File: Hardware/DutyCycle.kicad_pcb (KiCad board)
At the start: 2 copper layers, 40 x 20 mm, 42 parts, among them J1 LiPo, J2 USB, J4 MOT, Q1 AO3400A, Q2 AO3400A, Q3 AO3401A, SW1 SW_Push, U1 AT32F421KxU7, U3 ME6211C28M5, U5 TP4055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

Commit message: fix(Hardware): change the crystal starting capacitance 10pF -> 12pF
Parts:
- C10, C11: value 10pF -> 12pF

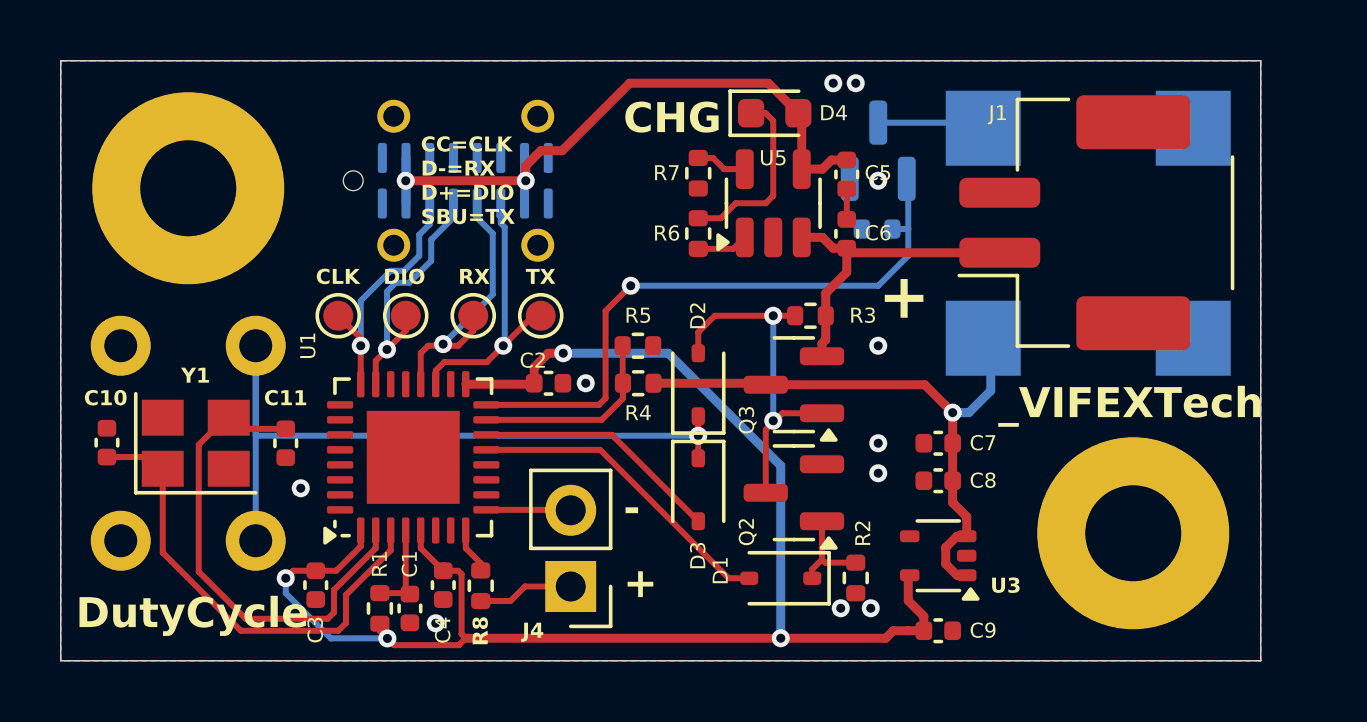
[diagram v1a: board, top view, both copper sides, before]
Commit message: feat(Hardware): add CH340E
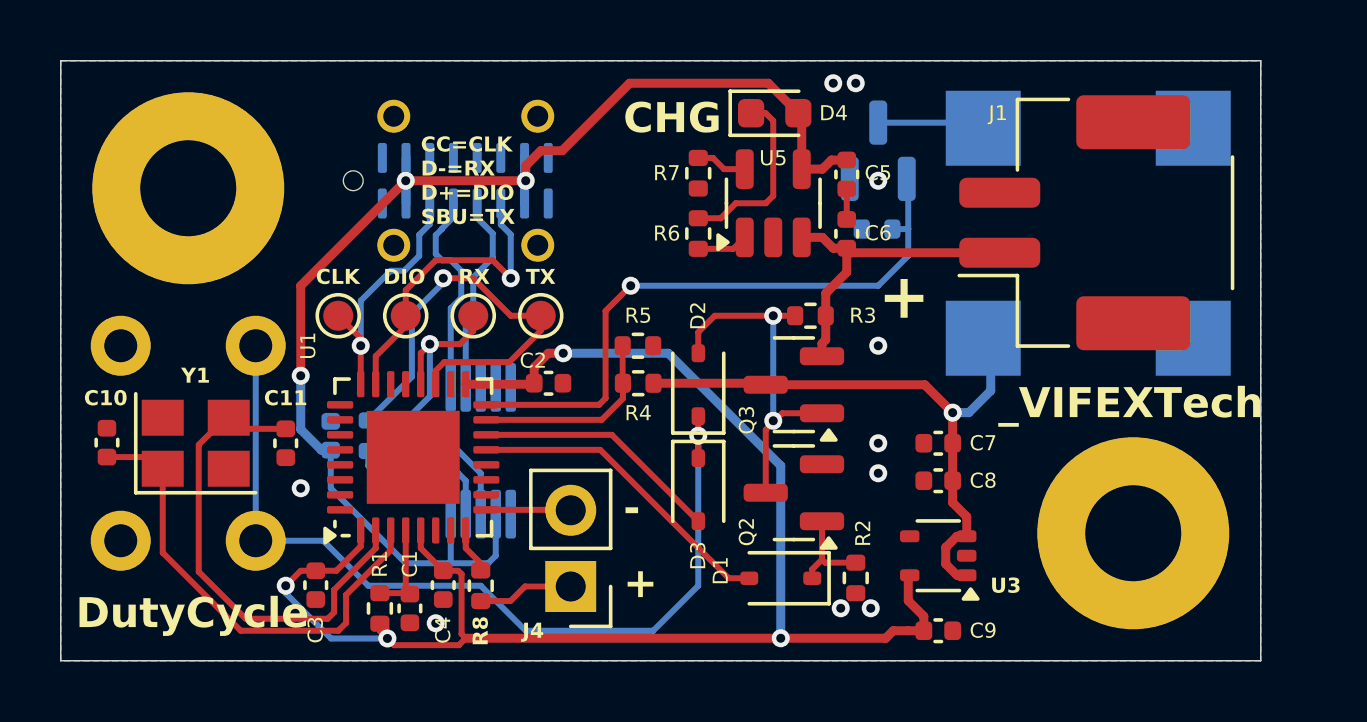
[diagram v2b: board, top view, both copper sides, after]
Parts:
- added C12: 100nF, Capacitor_SMD:C_0402_1005Metric, B.Cu at (84.0, 87.5)
- added R10: 10kR, Resistor_SMD:R_0402_1005Metric, B.Cu at (86.5, 87.5)
- added R11: 10kR, Resistor_SMD:R_0402_1005Metric, B.Cu at (85.2, 87.5)
- added U2: CH340E, Package_SO:MSOP-10_3x3mm_P0.5mm, B.Cu at (89.0, 88.0)
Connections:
- J2 pad A6: /SWDIO -> /UD+
- J2 pad A7: /DEBUG_RX -> /UD-
- J2 pad A8: /DEBUG_TX -> /SWDIO
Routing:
- net VBUS: track 21.8 -> 43.6 mm, vias 2 -> 3
- net /UD+: track 0.00 -> 7.04 mm
- net /UD-: track 0.00 -> 6.72 mm
- net Net-(U2-RXD): track 0.00 -> 5.06 mm
- net /DEBUG_TX: track 9.52 -> 14.5 mm
- net Net-(U2-TXD): track 0.00 -> 4.17 mm
- net Net-(D2-K): track 25.7 -> 29.5 mm
- net /DEBUG_RX: track 9.94 -> 6.97 mm
- net /SWDIO: track 8.80 -> 9.99 mm
- net /SWCLK: track 9.61 -> 8.90 mm
- net /HEXT_OUT: track 16.2 -> 15.6 mm
- net /HEXT_IN: track 15.8 -> 15.3 mm
- net GND: track 1.07 -> 1.02 mm, vias 11 -> 10

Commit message: fix(pcb): fix silk screen errors
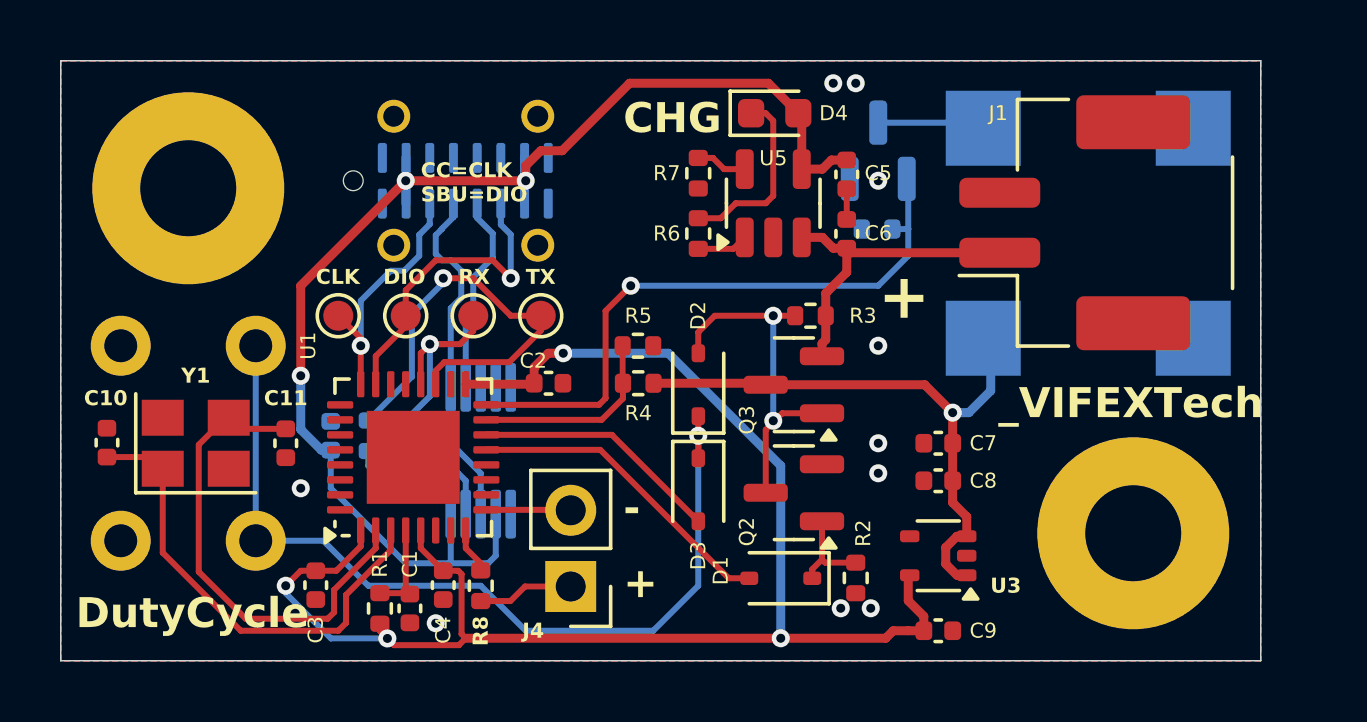
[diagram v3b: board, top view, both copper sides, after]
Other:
- board text added: "CC=CLK SBU=DIO"
- board text removed: "CC=CLK D-=RX D+=DIO SBU=TX"
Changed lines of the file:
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@@
 		)
 	)
-	(gr_text "CC=CLK\nD-=RX\nD+=DIO\nSBU=TX"
-		(at 87 80.5 0)
+	(gr_text "CC=CLK\nSBU=DIO"
+		(at 87 79.75 0)
 		(layer "F.SilkS")
 		(effects

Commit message: fix(pcb): fix buzzer not connect to pwm pin
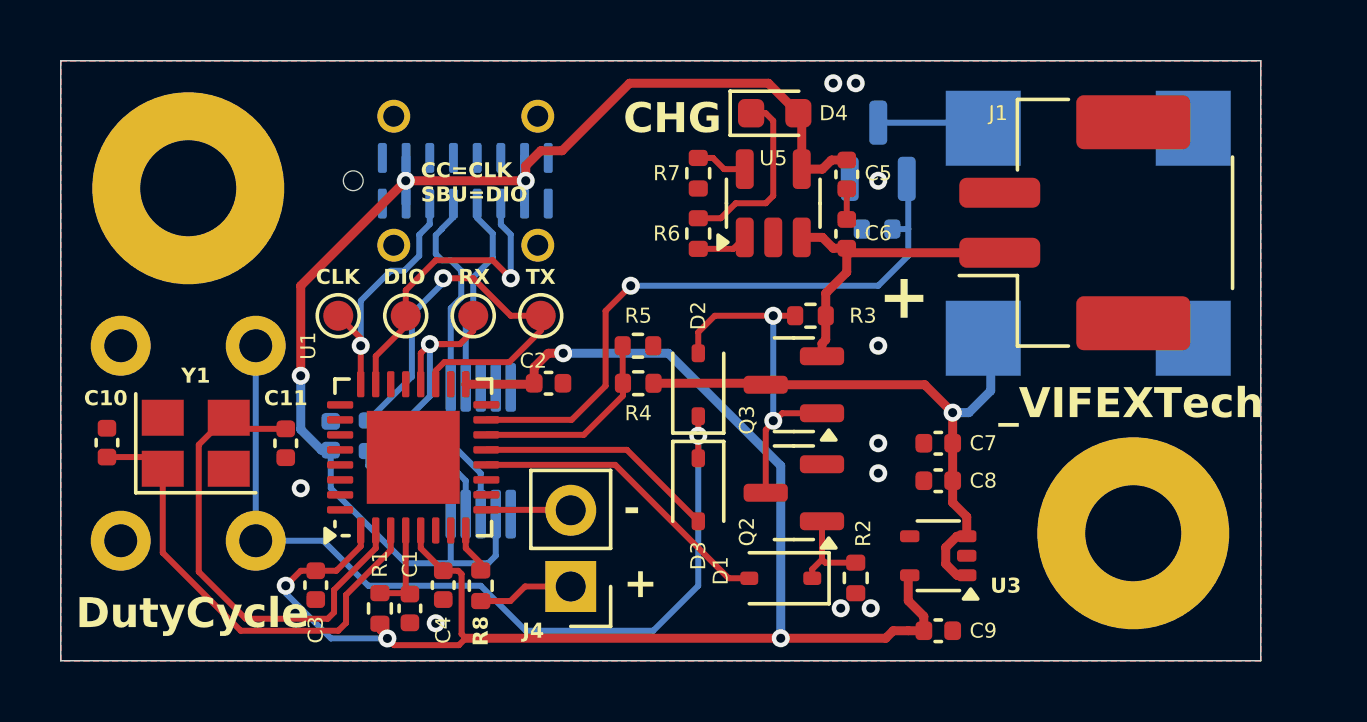
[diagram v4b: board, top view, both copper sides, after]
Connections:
- U1 pad 12: unconnected-(U1-PA6-Pad12) -> /PWR_EN
- U1 pad 13: /PWR_EN -> /KEY_DET
- U1 pad 14: /KEY_DET -> /BAT_DET
- U1 pad 15: /BAT_DET -> /BUZZ
- U1 pad 16: /BUZZ -> unconnected-(U1-PB2-Pad16)

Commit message: fix(Hardware): fix CH340E RES 10kR -> 100R
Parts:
- R10, R11: value 10kR -> 100R

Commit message: feat(Hardware): add support for USB insertion in both directions
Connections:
- J2 pad B5: unconnected-(J2-CC2-PadB5) -> /SWCLK
- J2 pad B6: unconnected-(J2-D+-PadB6) -> /UD+
- J2 pad B7: unconnected-(J2-D--PadB7) -> /UD-
- J2 pad B8: unconnected-(J2-SBU2-PadB8) -> /SWDIO
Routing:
- net VBUS: track 43.6 -> 55.8 mm
- net /SWDIO: track 9.99 -> 16.4 mm, vias 1 -> 3
- net /SWCLK: track 8.90 -> 13.2 mm, vias 1 -> 3
- net /UD+: track 7.04 -> 8.99 mm, vias 0 -> 2
- net /UD-: track 6.72 -> 8.39 mm
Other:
- board text added: "OPT"
